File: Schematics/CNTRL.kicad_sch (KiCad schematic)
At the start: 36 parts, among them SW1 RotaryEncoder_Switch, SW2 RotaryEncoder_Switch, SW3 RotaryEncoder_Switch, U5 PCA9555PW

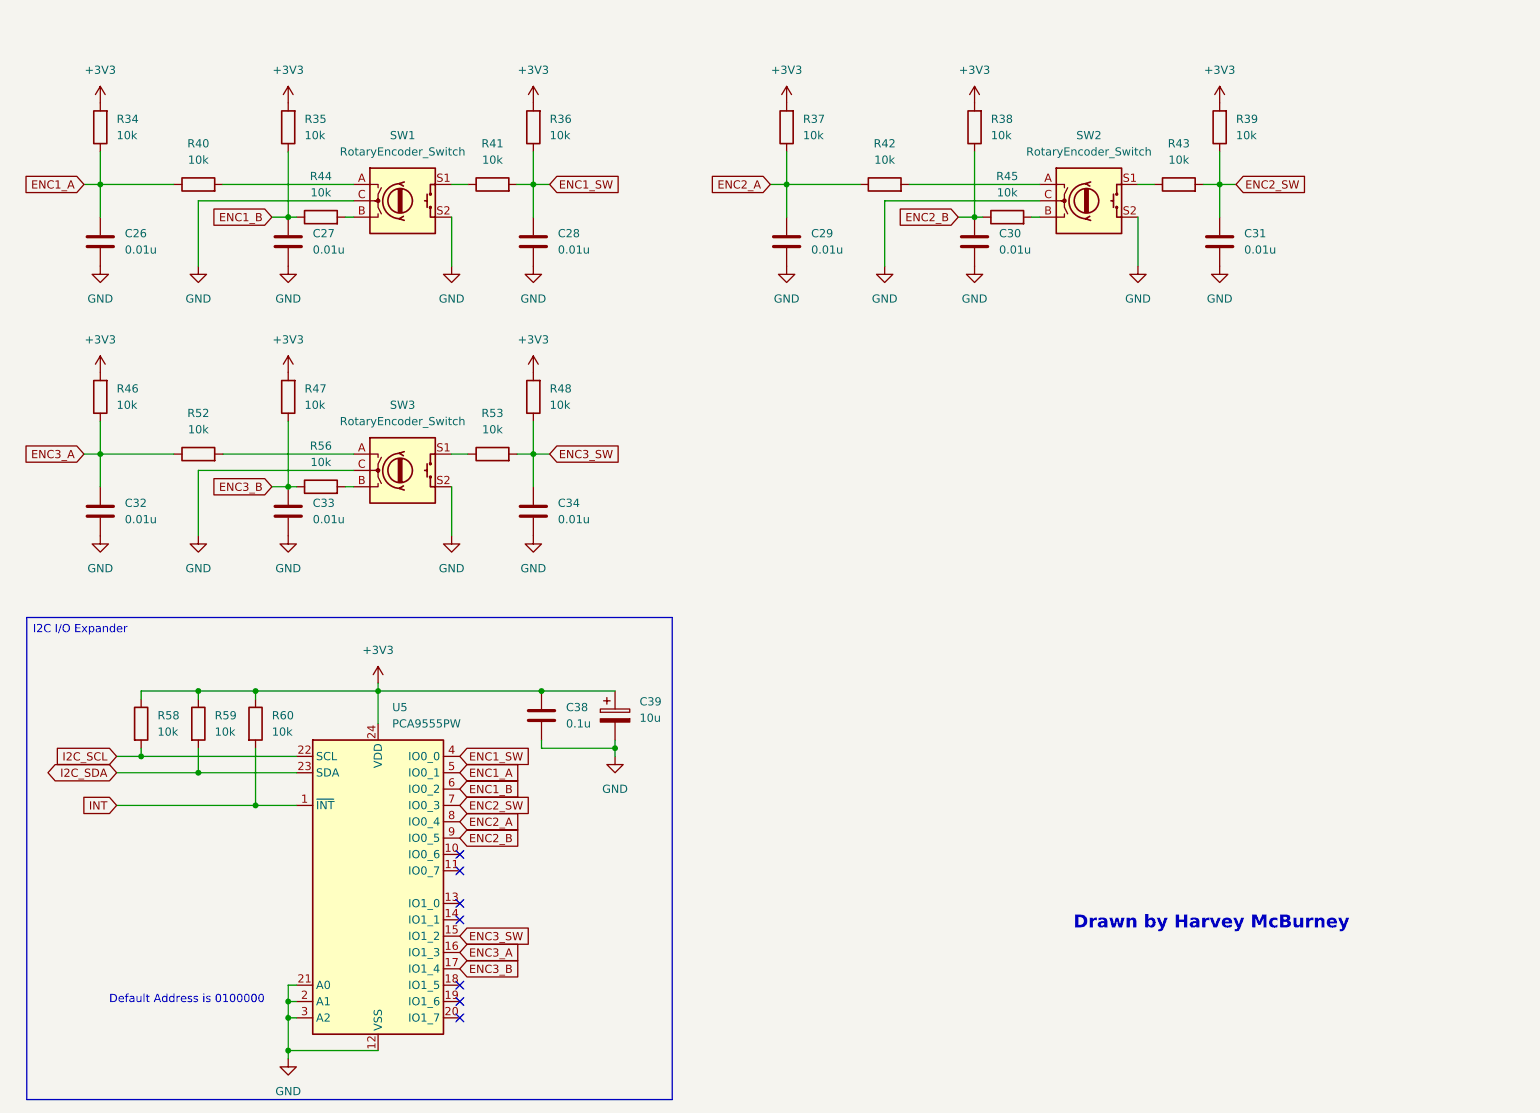
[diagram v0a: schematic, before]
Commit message: PCB design start
started on it :)
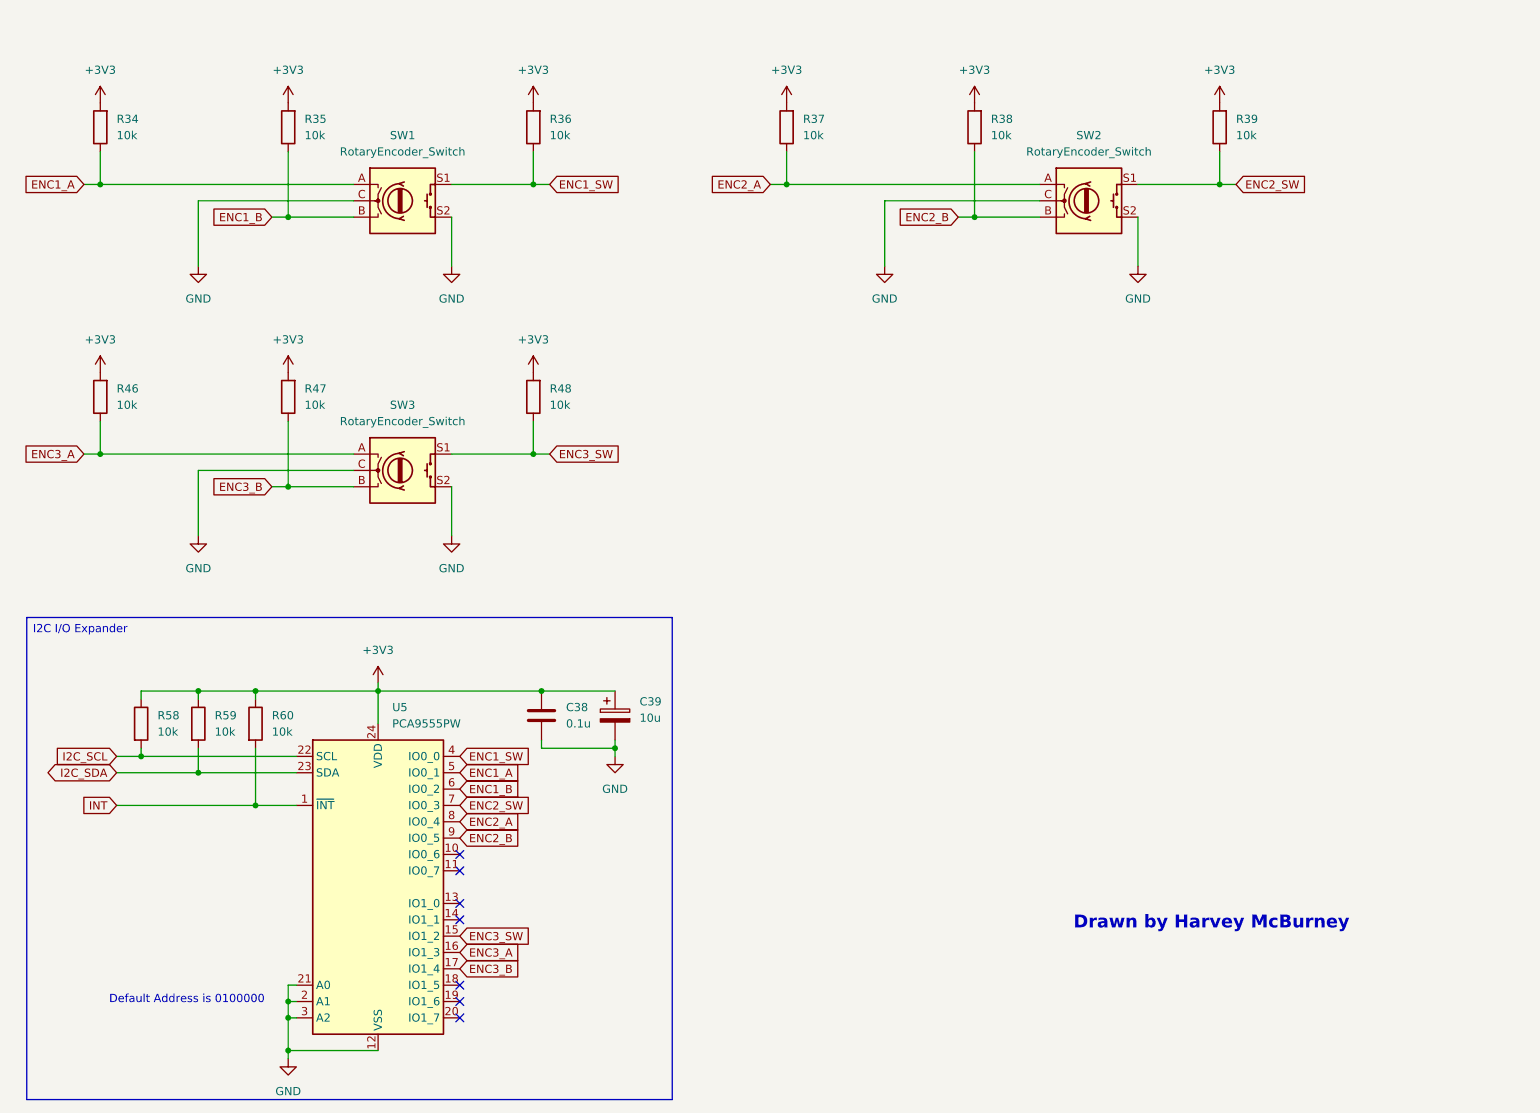
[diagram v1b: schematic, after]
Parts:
- removed C26, C27, C28, C29, C30, C31, C32, C33, C34: 0.01u, Capacitor_SMD:C_0805_2012Metric_Pad1.18x1.45mm_HandSolder, symbol Device:C
- removed R40, R41, R42, R43, R44, R45, R52, R53, R56: 10k, Resistor_SMD:R_0805_2012Metric_Pad1.20x1.40mm_HandSolder, symbol Device:R
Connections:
- net ENC1_A: now also SW1.A
- net ENC1_B: now also SW1.B
- net ENC1_SW: now also SW1.S1
- net ENC2_A: now also SW2.A
- net ENC2_B: now also SW2.B
- net ENC2_SW: now also SW2.S1
- net ENC3_A: now also SW3.A
- net ENC3_B: now also SW3.B
- net ENC3_SW: now also SW3.S1

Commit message: Fix for Uni PCB
CODEC module, DIP package, and through-hole less components
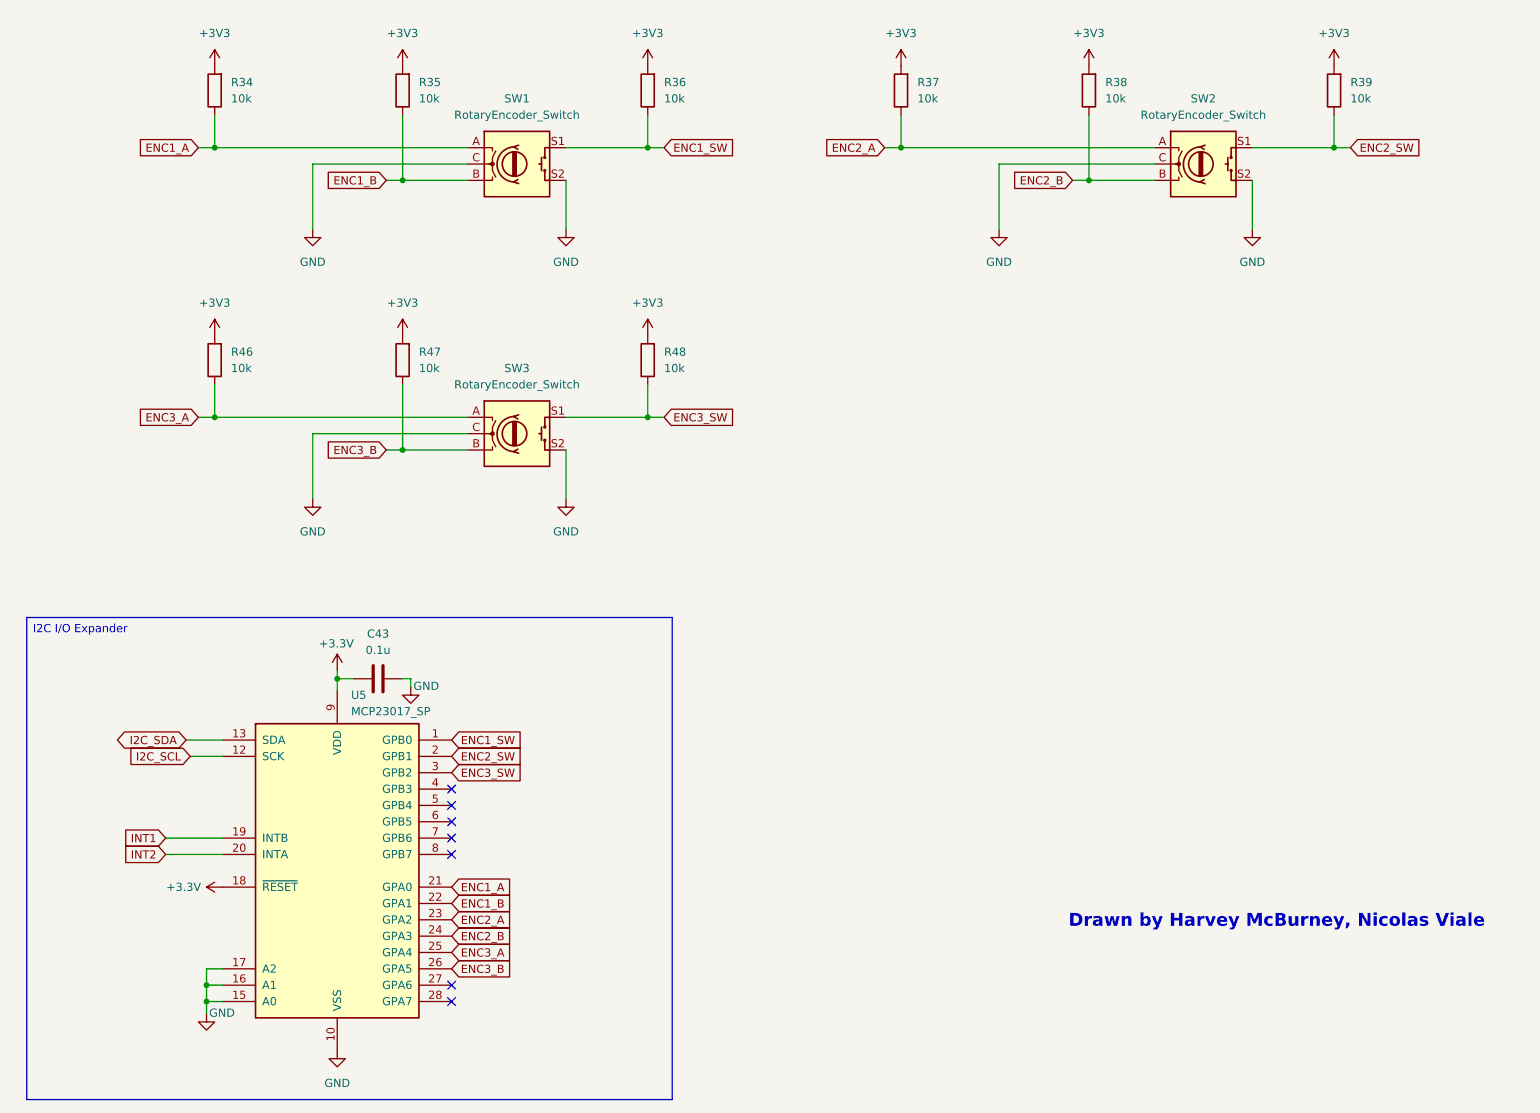
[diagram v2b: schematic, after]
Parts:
- removed C38: 0.1u, Capacitor_SMD:C_0805_2012Metric_Pad1.18x1.45mm_HandSolder, symbol Device:C
- removed C39: 10u, Capacitor_SMD:CP_Elec_4x5.7, symbol Device:C_Polarized
- removed R58, R59, R60: 10k, Resistor_SMD:R_0805_2012Metric_Pad1.20x1.40mm_HandSolder, symbol Device:R
- removed U5: PCA9555PW, Package_SO:TSSOP-24_4.4x7.8mm_P0.65mm, symbol Interface_Expansion:PCA9555PW
- added C43: 0.1u, Capacitor_SMD:C_0805_2012Metric_Pad1.18x1.45mm_HandSolder, symbol Device:C
- added U5: MCP23017_SP, Package_DIP:DIP-28_W7.62mm, symbol Interface_Expansion:MCP23017_SP
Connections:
- net ENC1_A: now also U5.21 (GPA0)
- net ENC1_B: now also U5.22 (GPA1)
- net ENC1_SW: now also U5.1 (GPB0)
- net ENC2_A: now also U5.23 (GPA2)
- net ENC2_B: now also U5.24 (GPA3)
- net ENC2_SW: now also U5.2 (GPB1)
- net ENC3_A: now also U5.25 (GPA4)
- net ENC3_B: now also U5.26 (GPA5)
- net ENC3_SW: now also U5.3 (GPB2)
- net GND: now also C43.1, U5.10 (VSS), U5.15 (A0), U5.16 (A1), U5.17 (A2)
- net I2C_SCL: now also U5.12 (SCK)
- net I2C_SDA: now also U5.13 (SDA)
- new net +3.3V: C43.2, U5.18 (~{RESET}), U5.9 (VDD)
- new net INT1: U5.19 (INTB)
- new net INT2: U5.20 (INTA)
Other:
- note added: "Drawn by Harvey McBurney, Nicolas Viale"
- note removed: "Default Address is 0100000"
- note removed: "Drawn by Harvey McBurney"
- moved on the sheet: R34, R35, R36, R37, R38, R39, R46, R47, R48, SW1, SW2, SW3
